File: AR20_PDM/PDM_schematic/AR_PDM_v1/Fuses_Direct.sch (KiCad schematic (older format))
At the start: 8 parts

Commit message: Major Schematics changes-work in progress
- Added rest of the phases
- Corrected pin names, and began to connect everything
- Began mapping the connectors, Pin-out not yet verified for all connectors
- Began mapping of user interface (Led indicators)
- INA233 now senses OUT voltage on mosfets instead of main 12Volt
- Added extra decoupling capacitors
Known things to fix:
- AUX inputs activation method, and a disconnect switch on phase 1-7 (mosfets)
- Rest of the user interface
- Find correct plugs for the system
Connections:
- net labels added: MCU_UNITS_FEED_OUT, V+12V
- net labels removed: ACM_FEED_OUT, VS_12V
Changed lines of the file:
@@
 $Descr A4 11693 8268
 encoding utf-8
-Sheet 4 6
+Sheet 3 11
 Title ""
 Date ""
@@
 Wire Wire Line
 	7750 3850 8950 3850
-Text HLabel 8950 2650 2    50   Input ~ 0
-ING_SWITCH_OUT
-Text HLabel 8950 2950 2    50   Input ~ 0
-ACM_FEED_OUT
-Text HLabel 8950 3250 2    50   Input ~ 0
+Text HLabel 8950 3250 2    50   Output ~ 0
 CLUTCH_ACT_OUT
-Text HLabel 8950 3550 2    50   Input ~ 0
-SHUTDOWN_OUT
-Text HLabel 8950 3850 2    50   Input ~ 0
+Text HLabel 8950 3850 2    50   Output ~ 0
 ETC_OUT
 Text Notes 5550 5800 0    50   ~ 10
@@
 $EndComp
 Text HLabel 2300 3000 0    50   Input ~ 0
-VS_12V
+V+12V
 $Comp
 L AR20_PDM_v1-rescue:R_Shunt-Device R?
@@
 Wire Wire Line
 	3200 3000 3250 3000
+Text HLabel 8950 3550 2    50   Output ~ 0
+SHUTDOWN_OUT
+Text HLabel 8950 2650 2    50   Output ~ 0
+ING_SWITCH_OUT
+Text HLabel 8950 2950 2    50   Output ~ 0
+MCU_UNITS_FEED_OUT
 $EndSCHEMATC

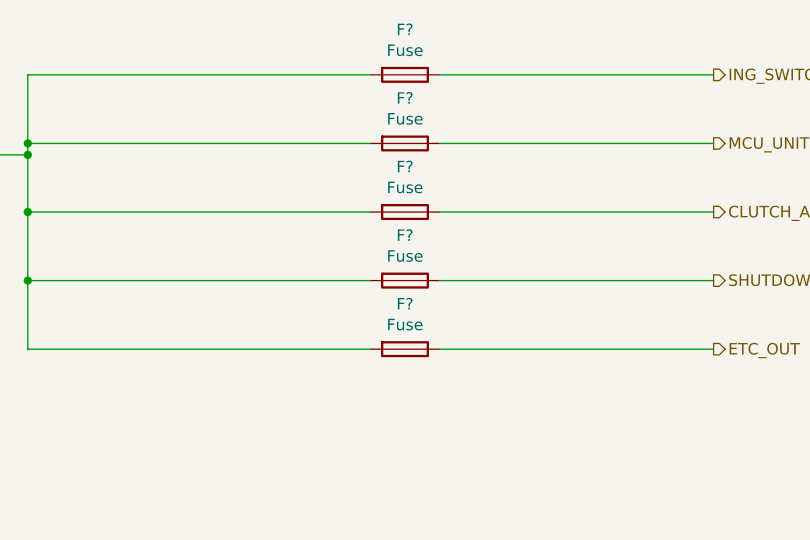
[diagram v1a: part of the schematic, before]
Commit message: Added LEDs and switches.
- Added all status leds
- Added all switches
- ! Connections are work in progress, not everything is correct
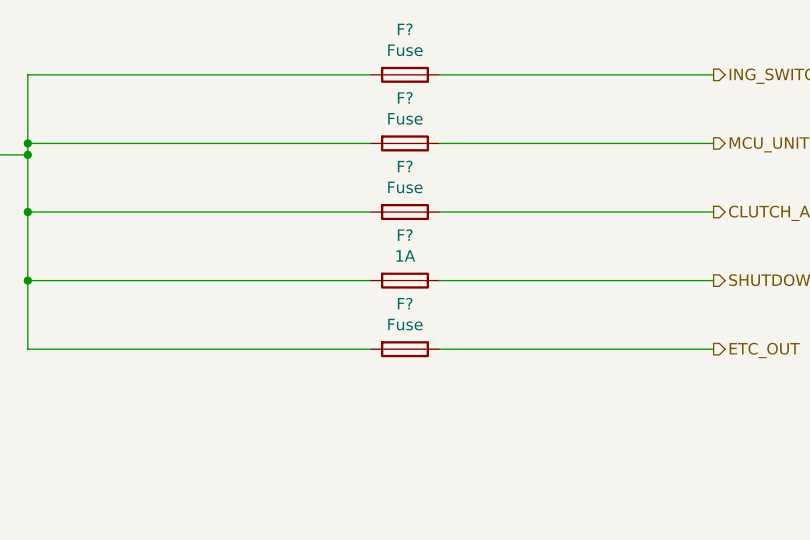
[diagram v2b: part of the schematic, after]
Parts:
- F?: value Fuse -> 1A
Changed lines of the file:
@@
 P 7600 3550
 F 0 "F?" V 7403 3550 50  0000 C CNN
-F 1 "Fuse" V 7494 3550 50  0000 C CNN
+F 1 "1A" V 7494 3550 50  0000 C CNN
 F 2 "" V 7530 3550 50  0001 C CNN
 F 3 "~" H 7600 3550 50  0001 C CNN

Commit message: Fixed issues, controlled components, BOM, see discription
- added acm symbol
- fixed wrongly faced P-mosfets
- I/O expander now sinks led instead of source
- Bill of material mostly done
- Correct address for INA233 chips.
- Now 4 diodes serves as flyback for all mosfets
- Corrected naming scheme for compmonents (everything is not fixed yet)
- Fixed some labels
- altso some minor changes
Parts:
- removed R?: R_Shunt-Device, symbol AR20_PDM_v1-rescue:R_Shunt-Device
- added R_Shunt3: 2m_1%_4W, symbol AR20_PDM_v1-rescue:R-Device
- C_bypass3: renamed from C_bypass?; value 0.1uF -> 100nf; footprint (none) -> Capacitor_SMD:C_0603_1608Metric
- gave numbers to parts that had none: 6
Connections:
- wire segments 40 -> 37
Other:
- note added: "addr: 1001001"
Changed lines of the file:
@@
 $EndDescr
 $Comp
-L Device:Fuse F?
+L Device:Fuse F1
 U 1 1 5DE4DAA4
 P 7600 2650
-F 0 "F?" V 7403 2650 50  0000 C CNN
+F 0 "F1" V 7403 2650 50  0000 C CNN
 F 1 "Fuse" V 7494 2650 50  0000 C CNN
 F 2 "" V 7530 2650 50  0001 C CNN
@@
 	7750 2650 8950 2650
 $Comp
-L Device:Fuse F?
+L Device:Fuse F2
 U 1 1 5DE4DAAD
 P 7600 2950
-F 0 "F?" V 7403 2950 50  0000 C CNN
+F 0 "F2" V 7403 2950 50  0000 C CNN
 F 1 "Fuse" V 7494 2950 50  0000 C CNN
 F 2 "" V 7530 2950 50  0001 C CNN
@@
 	7750 2950 8950 2950
 $Comp
-L Device:Fuse F?
+L Device:Fuse F3
 U 1 1 5DE4DAB6
 P 7600 3250
-F 0 "F?" V 7403 3250 50  0000 C CNN
+F 0 "F3" V 7403 3250 50  0000 C CNN
 F 1 "Fuse" V 7494 3250 50  0000 C CNN
 F 2 "" V 7530 3250 50  0001 C CNN
@@
 	7750 3250 8950 3250
 $Comp
-L Device:Fuse F?
+L Device:Fuse F4
 U 1 1 5DE4DABF
 P 7600 3550
-F 0 "F?" V 7403 3550 50  0000 C CNN
+F 0 "F4" V 7403 3550 50  0000 C CNN
 F 1 "1A" V 7494 3550 50  0000 C CNN
 F 2 "" V 7530 3550 50  0001 C CNN
@@
 	7750 3550 8950 3550
 $Comp
-L Device:Fuse F?
+L Device:Fuse F5
 U 1 1 5DE4DAC8
 P 7600 3850
-F 0 "F?" V 7403 3850 50  0000 C CNN
+F 0 "F5" V 7403 3850 50  0000 C CNN
 F 1 "Fuse" V 7494 3850 50  0000 C CNN
 F 2 "" V 7530 3850 50  0001 C CNN
@@
 Text HLabel 8950 3850 2    50   Output ~ 0
 ETC_OUT
-Text Notes 5550 5800 0    50   ~ 10
+Text Notes 5950 5650 0    50   ~ 10
 Configurable address, \nmust be different for each chip
 Wire Wire Line
 	5900 5500 5900 6000
-Wire Wire Line
-	5750 6000 5900 6000
-Connection ~ 5750 6000
-Wire Wire Line
-	5750 6000 5100 6000
-Connection ~ 5100 6000
-Wire Wire Line
-	5100 5750 5100 6000
-Wire Wire Line
-	5100 6000 5100 6200
 Wire Wire Line
 	5600 5400 6250 5400
@@
 AR Path="/5DA89415/5DE6C6C9" Ref="U?"  Part="1"
 AR Path="/5DA8920B/5DE6C6C9" Ref="U?"  Part="1"
-AR Path="/5DE4D361/5DE6C6C9" Ref="U?"  Part="1"
-F 0 "U?" H 5125 5515 50  0000 C CNN
+AR Path="/5DE4D361/5DE6C6C9" Ref="U4"  Part="1"
+F 0 "U4" H 5125 5515 50  0000 C CNN
 F 1 "INA233" H 5125 5424 50  0000 C CNN
 F 2 "" H 5100 5100 50  0001 C CNN
@@
 AR Path="/5DA89415/5DE6C6D8" Ref="#PWR?"  Part="1"
 AR Path="/5DA8920B/5DE6C6D8" Ref="#PWR?"  Part="1"
-AR Path="/5DE4D361/5DE6C6D8" Ref="#PWR?"  Part="1"
-F 0 "#PWR?" H 5100 5950 50  0001 C CNN
+AR Path="/5DE4D361/5DE6C6D8" Ref="#PWR025"  Part="1"
+F 0 "#PWR025" H 5100 5950 50  0001 C CNN
 F 1 "GND" H 5105 6027 50  0000 C CNN
 F 2 "" H 5100 6200 50  0001 C CNN
@@
 AR Path="/5DA89415/5DE6C6DF" Ref="#PWR?"  Part="1"
 AR Path="/5DA8920B/5DE6C6DF" Ref="#PWR?"  Part="1"
-AR Path="/5DE4D361/5DE6C6DF" Ref="#PWR?"  Part="1"
-F 0 "#PWR?" H 4200 4350 50  0001 C CNN
+AR Path="/5DE4D361/5DE6C6DF" Ref="#PWR024"  Part="1"
+F 0 "#PWR024" H 4200 4350 50  0001 C CNN
 F 1 "GND" V 4205 4472 50  0000 R CNN
 F 2 "" H 4200 4600 50  0001 C CNN
@@
 AR Path="/5DA89415/5DE6C6E5" Ref="C_bypass?"  Part="1"
 AR Path="/5DA8920B/5DE6C6E5" Ref="C_bypass?"  Part="1"
-AR Path="/5DE4D361/5DE6C6E5" Ref="C_bypass?"  Part="1"
-F 0 "C_bypass?" V 4148 4400 50  0000 C CNN
-F 1 "0.1uF" V 4239 4400 50  0000 C CNN
-F 2 "" H 4438 4250 50  0001 C CNN
+AR Path="/5DE4D361/5DE6C6E5" Ref="C_bypass3"  Part="1"
+F 0 "C_bypass3" V 4148 4400 50  0000 C CNN
+F 1 "100nf" V 4239 4400 50  0000 C CNN
+F 2 "Capacitor_SMD:C_0603_1608Metric" H 4438 4250 50  0001 C CNN
 F 3 "~" H 4400 4400 50  0001 C CNN
 	1    4400 4400
@@
 Text HLabel 2300 3000 0    50   Input ~ 0
 V+12V
-$Comp
-L AR20_PDM_v1-rescue:R_Shunt-Device R?
-U 1 1 5DE77FF4
-P 3450 3000
-AR Path="/5DA8920B/5DE77FF4" Ref="R?"  Part="1"
-AR Path="/5DE4D361/5DE77FF4" Ref="R?"  Part="1"
-F 0 "R?" V 3225 3000 50  0000 C CNN
-F 1 "R_Shunt-Device" V 3316 3000 50  0000 C CNN
-F 2 "" V 3380 3000 50  0001 C CNN
-F 3 "" H 3450 3000 50  0001 C CNN
-	1    3450 3000
-	0    1    1    0
-$EndComp
 Text Notes 2950 3300 0    50   ~ 0
 Place shunt close to INA233\n
@@
 	5950 3850 5950 3550
 Connection ~ 5950 3550
-Wire Wire Line
-	3650 3000 5950 3000
 Connection ~ 5950 3000
 Wire Wire Line
 	5950 3000 5950 2950
 Wire Wire Line
-	4650 5350 3350 5350
-Wire Wire Line
-	3350 5350 3350 3150
-Wire Wire Line
-	3550 3150 3550 5450
-Wire Wire Line
-	3550 5450 4650 5450
+	4650 5350 3300 5350
+Wire Wire Line
+	3600 5450 4650 5450
 Wire Wire Line
 	3200 5150 3200 3000
@@
 	3200 5150 4650 5150
 Connection ~ 3200 3000
-Wire Wire Line
-	3200 3000 3250 3000
 Text HLabel 8950 3550 2    50   Output ~ 0
 SHUTDOWN_OUT
@@
 Text HLabel 8950 2950 2    50   Output ~ 0
 MCU_UNITS_FEED_OUT
+$Comp
+L AR20_PDM_v1-rescue:R-Device R_Shunt?
+U 1 1 5E1E306F
+P 3450 3000
+AR Path="/5DA89415/5E1E306F" Ref="R_Shunt?"  Part="1"
+AR Path="/5DEB10A1/5E1E306F" Ref="R_Shunt?"  Part="1"
+AR Path="/5DEB20EA/5E1E306F" Ref="R_Shunt?"  Part="1"
+AR Path="/5E0E4725/5E1E306F" Ref="R_Shunt?"  Part="1"
+AR Path="/5E0E4A93/5E1E306F" Ref="R_Shunt?"  Part="1"
+AR Path="/5E0E4EB5/5E1E306F" Ref="R_Shunt?"  Part="1"
+AR Path="/5E0E5304/5E1E306F" Ref="R_Shunt?"  Part="1"
+AR Path="/5E0E594B/5E1E306F" Ref="R_Shunt?"  Part="1"
+AR Path="/5E0E607C/5E1E306F" Ref="R_Shunt?"  Part="1"
+AR Path="/5E0FB5C8/5E1E306F" Ref="R_Shunt?"  Part="1"
+AR Path="/5E0FBBBD/5E1E306F" Ref="R_Shunt?"  Part="1"
+AR Path="/5E0FC3A2/5E1E306F" Ref="R_Shunt?"  Part="1"
+AR Path="/5E0FCFDC/5E1E306F" Ref="R_Shunt?"  Part="1"
+AR Path="/5E0FDCCC/5E1E306F" Ref="R_Shunt?"  Part="1"
+AR Path="/5E10174B/5E1E306F" Ref="R_Shunt?"  Part="1"
+AR Path="/5DE4D361/5E1E306F" Ref="R_Shunt3"  Part="1"
+F 0 "R_Shunt3" V 3243 3000 50  0000 C CNN
+F 1 "2m_1%_4W" V 3334 3000 50  0000 C CNN
+F 2 "" V 3380 3000 50  0001 C CNN
+F 3 "~" H 3450 3000 50  0001 C CNN
+	1    3450 3000
+	0    1    1    0
+$EndComp
+Wire Wire Line
+	3600 3000 3600 5450
+Wire Wire Line
+	3600 3000 5950 3000
+Connection ~ 3600 3000
+Wire Wire Line
+	3200 3000 3300 3000
+Wire Wire Line
+	3300 3000 3300 5350
+Connection ~ 3300 3000
+Text Notes 5950 5800 0    50   ~ 0
+addr: 1001001
+Wire Wire Line
+	5100 5750 5100 6200
+Text HLabel 5750 6000 3    50   BiDi ~ 10
+DIRECT_SDA
+Text HLabel 5900 6000 3    50   Input ~ 10
+vcc_5v
 $EndSCHEMATC

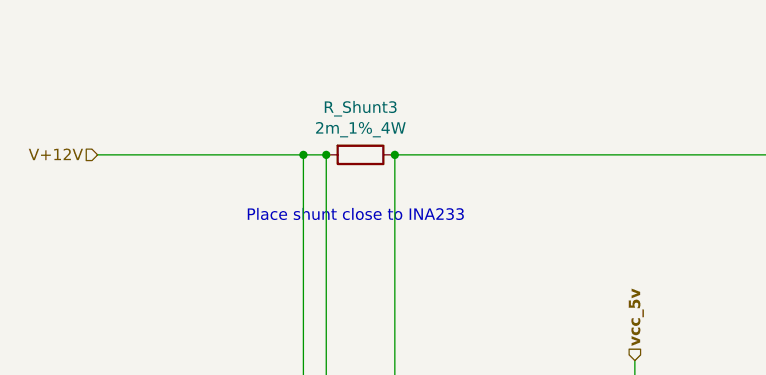
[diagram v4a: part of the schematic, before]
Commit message: PCB design, and issue fixing, work in progress
- Error fixed: Mux mosfet resistor change to ground
- Open drain output added on phase 6, for engine blipping purpose
- Most of pcb symbols and footprints are finished, including main connector
- PCB is change from 1oz to 2oz copper layer, for easier routing.
- Basic Draft of pcb is done, for now.
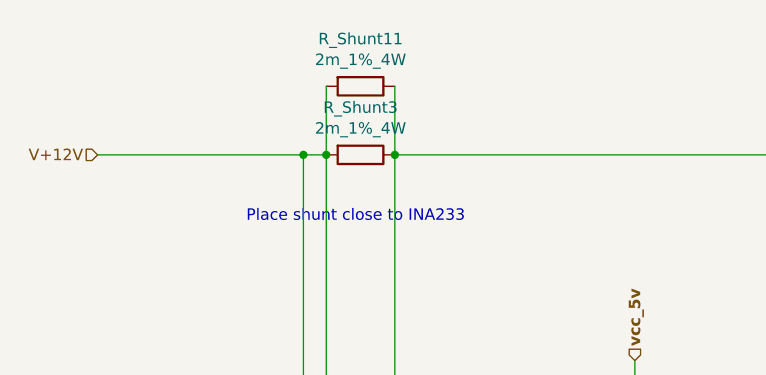
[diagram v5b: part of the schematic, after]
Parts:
- added R_Shunt11: 2m_1%_4W, Resistor_SMD:R_2512_6332Metric, symbol AR20_PDM_v1-rescue:R-Device
- F1, F2, F3, F4, F5: footprint (none) -> AR_PDM_v1:FuseHolder
- R_Shunt3: footprint (none) -> Resistor_SMD:R_2512_6332Metric
- U4: footprint (none) -> AR_PDM_v1:INA233
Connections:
- net V+12V: now also R_Shunt11.2
- net at F1.2, F2.2, F3.2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: now also R_Shunt11.1
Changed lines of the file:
@@
 F 0 "F1" V 7403 2650 50  0000 C CNN
 F 1 "Fuse" V 7494 2650 50  0000 C CNN
-F 2 "" V 7530 2650 50  0001 C CNN
+F 2 "AR_PDM_v1:FuseHolder" V 7530 2650 50  0001 C CNN
 F 3 "~" H 7600 2650 50  0001 C CNN
 	1    7600 2650
@@
 F 0 "F2" V 7403 2950 50  0000 C CNN
 F 1 "Fuse" V 7494 2950 50  0000 C CNN
-F 2 "" V 7530 2950 50  0001 C CNN
+F 2 "AR_PDM_v1:FuseHolder" V 7530 2950 50  0001 C CNN
 F 3 "~" H 7600 2950 50  0001 C CNN
 	1    7600 2950
@@
 F 0 "F3" V 7403 3250 50  0000 C CNN
 F 1 "Fuse" V 7494 3250 50  0000 C CNN
-F 2 "" V 7530 3250 50  0001 C CNN
+F 2 "AR_PDM_v1:FuseHolder" V 7530 3250 50  0001 C CNN
 F 3 "~" H 7600 3250 50  0001 C CNN
 	1    7600 3250
@@
 F 0 "F4" V 7403 3550 50  0000 C CNN
 F 1 "1A" V 7494 3550 50  0000 C CNN
-F 2 "" V 7530 3550 50  0001 C CNN
+F 2 "AR_PDM_v1:FuseHolder" V 7530 3550 50  0001 C CNN
 F 3 "~" H 7600 3550 50  0001 C CNN
 	1    7600 3550
@@
 F 0 "F5" V 7403 3850 50  0000 C CNN
 F 1 "Fuse" V 7494 3850 50  0000 C CNN
-F 2 "" V 7530 3850 50  0001 C CNN
+F 2 "AR_PDM_v1:FuseHolder" V 7530 3850 50  0001 C CNN
 F 3 "~" H 7600 3850 50  0001 C CNN
 	1    7600 3850
@@
 F 0 "U4" H 5125 5515 50  0000 C CNN
 F 1 "INA233" H 5125 5424 50  0000 C CNN
-F 2 "" H 5100 5100 50  0001 C CNN
+F 2 "AR_PDM_v1:INA233" H 5100 5100 50  0001 C CNN
 F 3 "" H 5100 5100 50  0001 C CNN
 	1    5100 5100
@@
 F 0 "R_Shunt3" V 3243 3000 50  0000 C CNN
 F 1 "2m_1%_4W" V 3334 3000 50  0000 C CNN
-F 2 "" V 3380 3000 50  0001 C CNN
+F 2 "Resistor_SMD:R_2512_6332Metric" V 3380 3000 50  0001 C CNN
 F 3 "~" H 3450 3000 50  0001 C CNN
 	1    3450 3000
@@
 Text HLabel 5900 6000 3    50   Input ~ 10
 vcc_5v
+$Comp
+L AR20_PDM_v1-rescue:R-Device R_Shunt?
+U 1 1 5E24C0CF
+P 3450 2700
+AR Path="/5DA89415/5E24C0CF" Ref="R_Shunt?"  Part="1"
+AR Path="/5DEB10A1/5E24C0CF" Ref="R_Shunt?"  Part="1"
+AR Path="/5DEB20EA/5E24C0CF" Ref="R_Shunt?"  Part="1"
+AR Path="/5E0E4725/5E24C0CF" Ref="R_Shunt?"  Part="1"
+AR Path="/5E0E4A93/5E24C0CF" Ref="R_Shunt?"  Part="1"
+AR Path="/5E0E4EB5/5E24C0CF" Ref="R_Shunt?"  Part="1"
+AR Path="/5E0E5304/5E24C0CF" Ref="R_Shunt?"  Part="1"
+AR Path="/5E0E594B/5E24C0CF" Ref="R_Shunt?"  Part="1"
+AR Path="/5E0E607C/5E24C0CF" Ref="R_Shunt?"  Part="1"
+AR Path="/5E0FB5C8/5E24C0CF" Ref="R_Shunt?"  Part="1"
+AR Path="/5E0FBBBD/5E24C0CF" Ref="R_Shunt?"  Part="1"
+AR Path="/5E0FC3A2/5E24C0CF" Ref="R_Shunt?"  Part="1"
+AR Path="/5E0FCFDC/5E24C0CF" Ref="R_Shunt?"  Part="1"
+AR Path="/5E0FDCCC/5E24C0CF" Ref="R_Shunt?"  Part="1"
+AR Path="/5E10174B/5E24C0CF" Ref="R_Shunt?"  Part="1"
+AR Path="/5DE4D361/5E24C0CF" Ref="R_Shunt11"  Part="1"
+F 0 "R_Shunt11" V 3243 2700 50  0000 C CNN
+F 1 "2m_1%_4W" V 3334 2700 50  0000 C CNN
+F 2 "Resistor_SMD:R_2512_6332Metric" V 3380 2700 50  0001 C CNN
+F 3 "~" H 3450 2700 50  0001 C CNN
+	1    3450 2700
+	0    1    1    0
+$EndComp
+Wire Wire Line
+	3300 3000 3300 2700
+Wire Wire Line
+	3600 3000 3600 2700
 $EndSCHEMATC

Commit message: Alpha version DONE! - Gerber files generated
- Tweeked
- checked and re cheked
- added all missing components
- Created a really nice silkscreen
- Ready To Test
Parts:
- renumbered C_bypass3 to C46, R_Shunt3 to R100, R_Shunt11 to R99, U4 to U31
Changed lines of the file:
@@
 AR Path="/5DA89415/5DE6C6C9" Ref="U?"  Part="1"
 AR Path="/5DA8920B/5DE6C6C9" Ref="U?"  Part="1"
-AR Path="/5DE4D361/5DE6C6C9" Ref="U4"  Part="1"
-F 0 "U4" H 5125 5515 50  0000 C CNN
+AR Path="/5DE4D361/5DE6C6C9" Ref="U31"  Part="1"
+F 0 "U31" H 5125 5515 50  0000 C CNN
 F 1 "INA233" H 5125 5424 50  0000 C CNN
 F 2 "AR_PDM_v1:INA233" H 5100 5100 50  0001 C CNN
@@
 AR Path="/5DA89415/5DE6C6D8" Ref="#PWR?"  Part="1"
 AR Path="/5DA8920B/5DE6C6D8" Ref="#PWR?"  Part="1"
-AR Path="/5DE4D361/5DE6C6D8" Ref="#PWR025"  Part="1"
-F 0 "#PWR025" H 5100 5950 50  0001 C CNN
+AR Path="/5DE4D361/5DE6C6D8" Ref="#PWR0126"  Part="1"
+F 0 "#PWR0126" H 5100 5950 50  0001 C CNN
 F 1 "GND" H 5105 6027 50  0000 C CNN
 F 2 "" H 5100 6200 50  0001 C CNN
@@
 AR Path="/5DA89415/5DE6C6DF" Ref="#PWR?"  Part="1"
 AR Path="/5DA8920B/5DE6C6DF" Ref="#PWR?"  Part="1"
-AR Path="/5DE4D361/5DE6C6DF" Ref="#PWR024"  Part="1"
-F 0 "#PWR024" H 4200 4350 50  0001 C CNN
+AR Path="/5DE4D361/5DE6C6DF" Ref="#PWR0125"  Part="1"
+F 0 "#PWR0125" H 4200 4350 50  0001 C CNN
 F 1 "GND" V 4205 4472 50  0000 R CNN
 F 2 "" H 4200 4600 50  0001 C CNN
@@
 $EndComp
 $Comp
-L AR20_PDM_v1-rescue:C-Device C_bypass?
+L AR20_PDM_v1-rescue:C-Device C?
 U 1 1 5DE6C6E5
 P 4400 4400
-AR Path="/5DA89415/5DE6C6E5" Ref="C_bypass?"  Part="1"
-AR Path="/5DA8920B/5DE6C6E5" Ref="C_bypass?"  Part="1"
-AR Path="/5DE4D361/5DE6C6E5" Ref="C_bypass3"  Part="1"
-F 0 "C_bypass3" V 4148 4400 50  0000 C CNN
+AR Path="/5DA89415/5DE6C6E5" Ref="C?"  Part="1"
+AR Path="/5DA8920B/5DE6C6E5" Ref="C?"  Part="1"
+AR Path="/5DE4D361/5DE6C6E5" Ref="C46"  Part="1"
+F 0 "C46" V 4148 4400 50  0000 C CNN
 F 1 "100nf" V 4239 4400 50  0000 C CNN
 F 2 "Capacitor_SMD:C_0603_1608Metric" H 4438 4250 50  0001 C CNN
@@
 MCU_UNITS_FEED_OUT
 $Comp
-L AR20_PDM_v1-rescue:R-Device R_Shunt?
+L AR20_PDM_v1-rescue:R-Device R?
 U 1 1 5E1E306F
 P 3450 3000
-AR Path="/5DA89415/5E1E306F" Ref="R_Shunt?"  Part="1"
-AR Path="/5DEB10A1/5E1E306F" Ref="R_Shunt?"  Part="1"
-AR Path="/5DEB20EA/5E1E306F" Ref="R_Shunt?"  Part="1"
-AR Path="/5E0E4725/5E1E306F" Ref="R_Shunt?"  Part="1"
-AR Path="/5E0E4A93/5E1E306F" Ref="R_Shunt?"  Part="1"
-AR Path="/5E0E4EB5/5E1E306F" Ref="R_Shunt?"  Part="1"
-AR Path="/5E0E5304/5E1E306F" Ref="R_Shunt?"  Part="1"
-AR Path="/5E0E594B/5E1E306F" Ref="R_Shunt?"  Part="1"
-AR Path="/5E0E607C/5E1E306F" Ref="R_Shunt?"  Part="1"
-AR Path="/5E0FB5C8/5E1E306F" Ref="R_Shunt?"  Part="1"
-AR Path="/5E0FBBBD/5E1E306F" Ref="R_Shunt?"  Part="1"
-AR Path="/5E0FC3A2/5E1E306F" Ref="R_Shunt?"  Part="1"
-AR Path="/5E0FCFDC/5E1E306F" Ref="R_Shunt?"  Part="1"
-AR Path="/5E0FDCCC/5E1E306F" Ref="R_Shunt?"  Part="1"
-AR Path="/5E10174B/5E1E306F" Ref="R_Shunt?"  Part="1"
-AR Path="/5DE4D361/5E1E306F" Ref="R_Shunt3"  Part="1"
-F 0 "R_Shunt3" V 3243 3000 50  0000 C CNN
+AR Path="/5DA89415/5E1E306F" Ref="R?"  Part="1"
+AR Path="/5DEB10A1/5E1E306F" Ref="R?"  Part="1"
+AR Path="/5DEB20EA/5E1E306F" Ref="R?"  Part="1"
+AR Path="/5E0E4725/5E1E306F" Ref="R?"  Part="1"
+AR Path="/5E0E4A93/5E1E306F" Ref="R?"  Part="1"
+AR Path="/5E0E4EB5/5E1E306F" Ref="R?"  Part="1"
+AR Path="/5E0E5304/5E1E306F" Ref="R?"  Part="1"
+AR Path="/5E0E594B/5E1E306F" Ref="R?"  Part="1"
+AR Path="/5E0E607C/5E1E306F" Ref="R?"  Part="1"
+AR Path="/5E0FB5C8/5E1E306F" Ref="R?"  Part="1"
+AR Path="/5E0FBBBD/5E1E306F" Ref="R?"  Part="1"
+AR Path="/5E0FC3A2/5E1E306F" Ref="R?"  Part="1"
+AR Path="/5E0FCFDC/5E1E306F" Ref="R?"  Part="1"
+AR Path="/5E0FDCCC/5E1E306F" Ref="R?"  Part="1"
+AR Path="/5E10174B/5E1E306F" Ref="R?"  Part="1"
+AR Path="/5DE4D361/5E1E306F" Ref="R100"  Part="1"
+F 0 "R100" V 3243 3000 50  0000 C CNN
 F 1 "2m_1%_4W" V 3334 3000 50  0000 C CNN
 F 2 "Resistor_SMD:R_2512_6332Metric" V 3380 3000 50  0001 C CNN
@@
 vcc_5v
 $Comp
-L AR20_PDM_v1-rescue:R-Device R_Shunt?
+L AR20_PDM_v1-rescue:R-Device R?
 U 1 1 5E24C0CF
 P 3450 2700
-AR Path="/5DA89415/5E24C0CF" Ref="R_Shunt?"  Part="1"
-AR Path="/5DEB10A1/5E24C0CF" Ref="R_Shunt?"  Part="1"
-AR Path="/5DEB20EA/5E24C0CF" Ref="R_Shunt?"  Part="1"
-AR Path="/5E0E4725/5E24C0CF" Ref="R_Shunt?"  Part="1"
-AR Path="/5E0E4A93/5E24C0CF" Ref="R_Shunt?"  Part="1"
-AR Path="/5E0E4EB5/5E24C0CF" Ref="R_Shunt?"  Part="1"
-AR Path="/5E0E5304/5E24C0CF" Ref="R_Shunt?"  Part="1"
-AR Path="/5E0E594B/5E24C0CF" Ref="R_Shunt?"  Part="1"
-AR Path="/5E0E607C/5E24C0CF" Ref="R_Shunt?"  Part="1"
-AR Path="/5E0FB5C8/5E24C0CF" Ref="R_Shunt?"  Part="1"
-AR Path="/5E0FBBBD/5E24C0CF" Ref="R_Shunt?"  Part="1"
-AR Path="/5E0FC3A2/5E24C0CF" Ref="R_Shunt?"  Part="1"
-AR Path="/5E0FCFDC/5E24C0CF" Ref="R_Shunt?"  Part="1"
-AR Path="/5E0FDCCC/5E24C0CF" Ref="R_Shunt?"  Part="1"
-AR Path="/5E10174B/5E24C0CF" Ref="R_Shunt?"  Part="1"
-AR Path="/5DE4D361/5E24C0CF" Ref="R_Shunt11"  Part="1"
-F 0 "R_Shunt11" V 3243 2700 50  0000 C CNN
+AR Path="/5DA89415/5E24C0CF" Ref="R?"  Part="1"
+AR Path="/5DEB10A1/5E24C0CF" Ref="R?"  Part="1"
+AR Path="/5DEB20EA/5E24C0CF" Ref="R?"  Part="1"
+AR Path="/5E0E4725/5E24C0CF" Ref="R?"  Part="1"
+AR Path="/5E0E4A93/5E24C0CF" Ref="R?"  Part="1"
+AR Path="/5E0E4EB5/5E24C0CF" Ref="R?"  Part="1"
+AR Path="/5E0E5304/5E24C0CF" Ref="R?"  Part="1"
+AR Path="/5E0E594B/5E24C0CF" Ref="R?"  Part="1"
+AR Path="/5E0E607C/5E24C0CF" Ref="R?"  Part="1"
+AR Path="/5E0FB5C8/5E24C0CF" Ref="R?"  Part="1"
+AR Path="/5E0FBBBD/5E24C0CF" Ref="R?"  Part="1"
+AR Path="/5E0FC3A2/5E24C0CF" Ref="R?"  Part="1"
+AR Path="/5E0FCFDC/5E24C0CF" Ref="R?"  Part="1"
+AR Path="/5E0FDCCC/5E24C0CF" Ref="R?"  Part="1"
+AR Path="/5E10174B/5E24C0CF" Ref="R?"  Part="1"
+AR Path="/5DE4D361/5E24C0CF" Ref="R99"  Part="1"
+F 0 "R99" V 3243 2700 50  0000 C CNN
 F 1 "2m_1%_4W" V 3334 2700 50  0000 C CNN
 F 2 "Resistor_SMD:R_2512_6332Metric" V 3380 2700 50  0001 C CNN
